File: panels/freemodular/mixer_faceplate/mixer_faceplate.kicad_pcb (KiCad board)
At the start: 2 copper layers, 40.3 x 128.5 mm, 0 parts

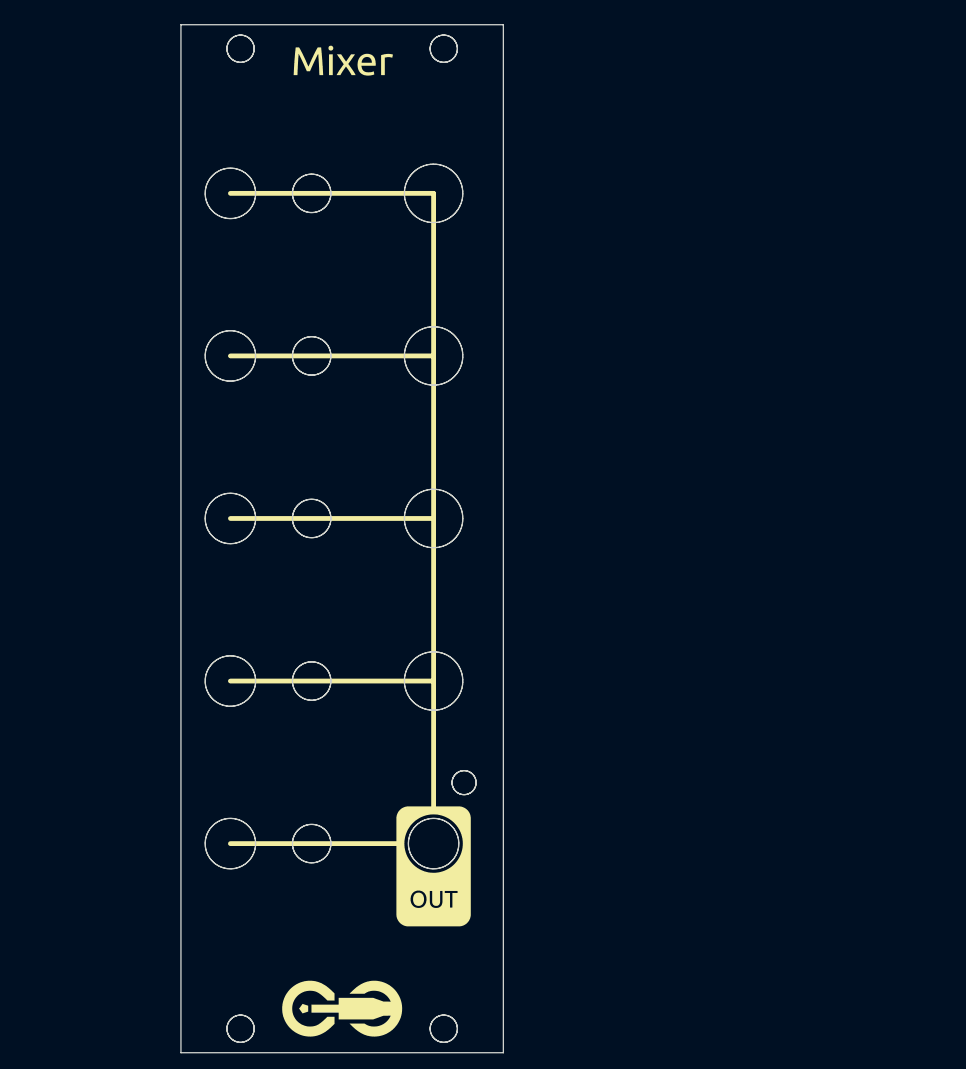
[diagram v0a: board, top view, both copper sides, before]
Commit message: mod2 firmwares, new faceplates
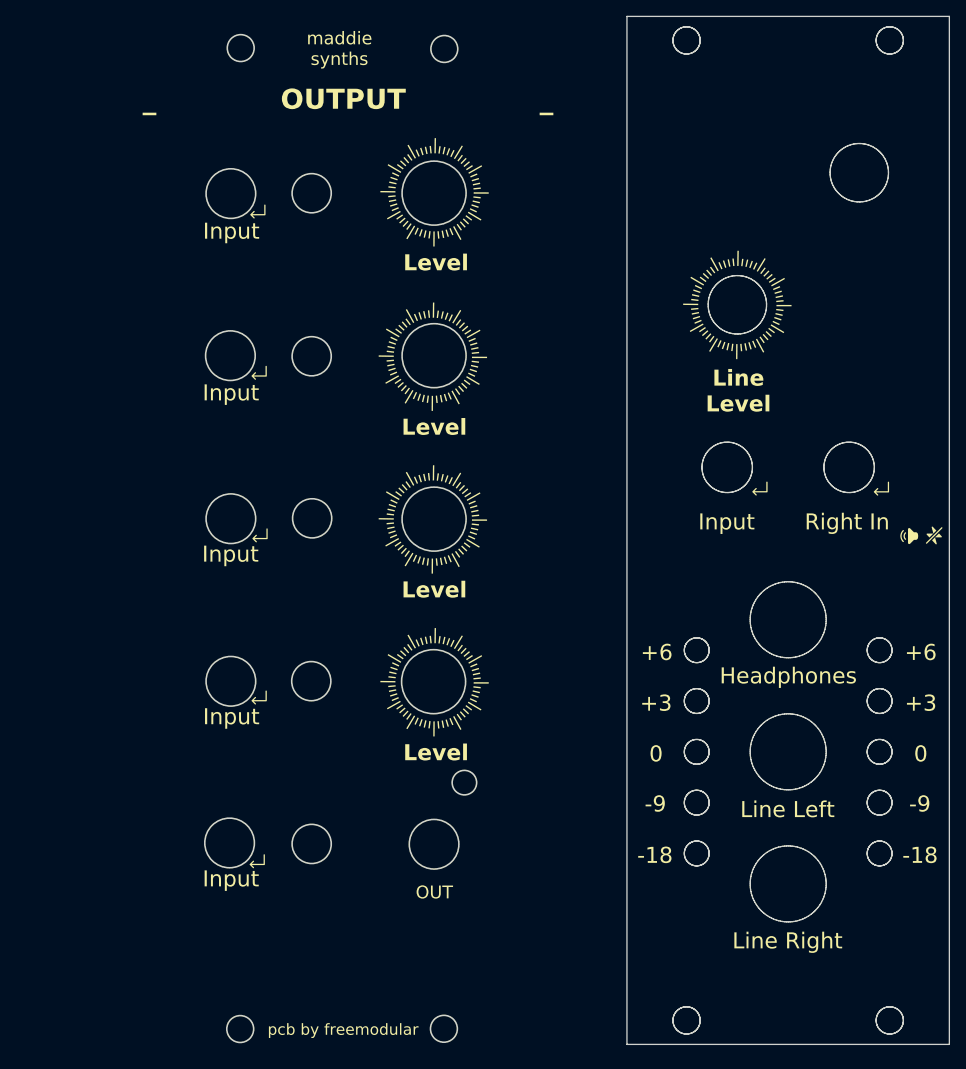
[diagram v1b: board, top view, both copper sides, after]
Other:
- board size 40.3 x 128.5 mm -> 93.1 x 128.5 mm
- board text added: "+3"
- board text added: "+6"
- board text added: "-18"
- board text added: "-9"
- board text added: "0"
- board text added: "Headphones"
- board text added: "Input"
- board text added: "Level"
- board text added: "Line Left"
- board text added: "Line Level"
- board text added: "Line Right"
- board text added: "OUT"
- board text added: "Right In"
- board text added: "_ OUTPUT _"
- board text added: "maddie synths"
- board text added: "pcb by freemodular"
